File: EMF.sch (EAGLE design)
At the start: 23 parts, among them X1 22-23-2021

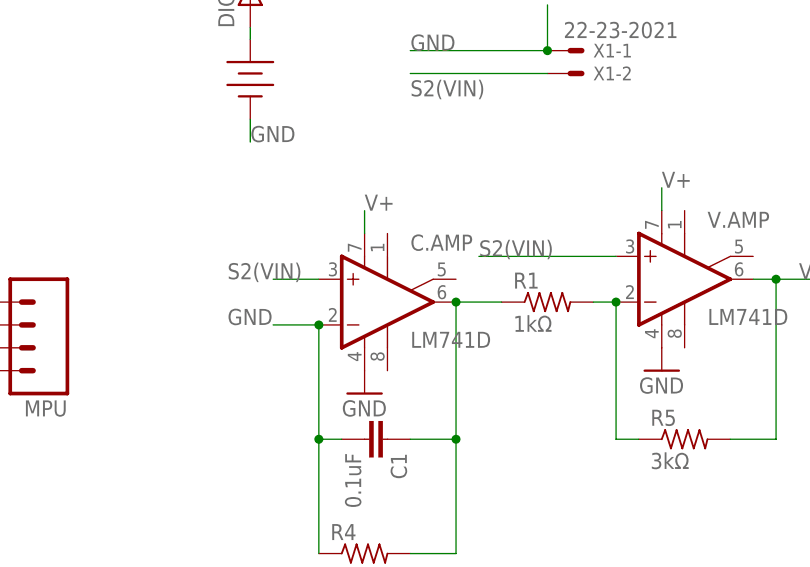
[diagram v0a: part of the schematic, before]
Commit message: fix op-amp connections
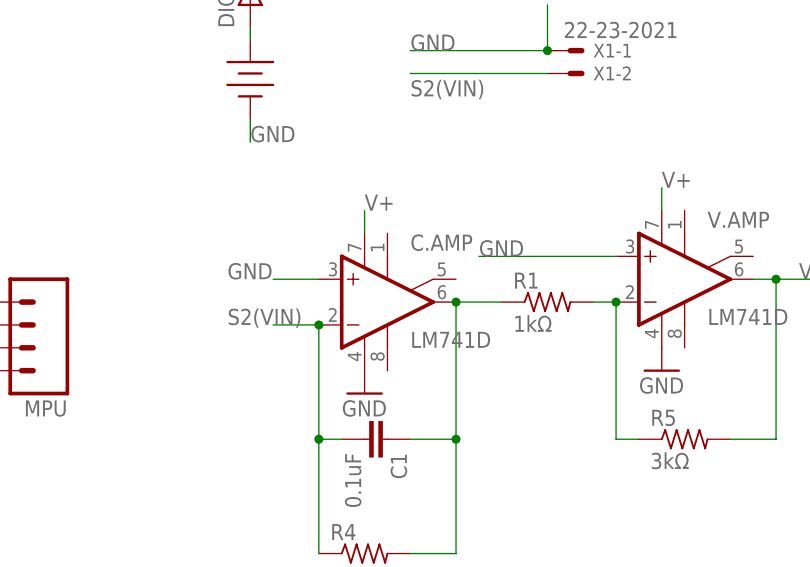
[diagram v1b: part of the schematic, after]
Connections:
- net GND: now also C.AMP.+IN, V.AMP.+IN; no longer C.AMP.-IN, C1.2, R4.1
- net S2(VIN): now also C.AMP.-IN, C1.2, R4.1; no longer C.AMP.+IN, V.AMP.+IN
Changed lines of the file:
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@@
 </segment>
 <segment>
-<pinref part="C.AMP" gate="A" pin="+IN"/>
-<wire x1="30.48" y1="55.88" x2="25.4" y2="55.88" width="0.1524" layer="91"/>
-<label x="20.32" y="55.88" size="1.778" layer="95"/>
-</segment>
-<segment>
-<pinref part="V.AMP" gate="A" pin="+IN"/>
-<wire x1="63.5" y1="58.42" x2="48.26" y2="58.42" width="0.1524" layer="91"/>
-<label x="48.26" y="58.42" size="1.778" layer="95"/>
+<pinref part="C.AMP" gate="A" pin="-IN"/>
+<wire x1="30.48" y1="50.8" x2="25.4" y2="50.8" width="0.1524" layer="91"/>
+<label x="20.32" y="50.8" size="1.778" layer="95"/>
+<wire x1="30.48" y1="50.8" x2="30.48" y2="38.1" width="0.1524" layer="91"/>
+<junction x="30.48" y="50.8"/>
+<pinref part="C1" gate="G$1" pin="2"/>
+<wire x1="30.48" y1="38.1" x2="33.02" y2="38.1" width="0.1524" layer="91"/>
+<pinref part="R4" gate="G$1" pin="1"/>
+<wire x1="30.48" y1="38.1" x2="30.48" y2="25.4" width="0.1524" layer="91"/>
+<junction x="30.48" y="38.1"/>
 </segment>
 </net>
@@
 </segment>
 <segment>
-<pinref part="C.AMP" gate="A" pin="-IN"/>
-<wire x1="30.48" y1="50.8" x2="25.4" y2="50.8" width="0.1524" layer="91"/>
-<label x="20.32" y="50.8" size="1.778" layer="95"/>
-<wire x1="30.48" y1="50.8" x2="30.48" y2="38.1" width="0.1524" layer="91"/>
-<junction x="30.48" y="50.8"/>
-<pinref part="C1" gate="G$1" pin="2"/>
-<wire x1="30.48" y1="38.1" x2="33.02" y2="38.1" width="0.1524" layer="91"/>
-<pinref part="R4" gate="G$1" pin="1"/>
-<wire x1="30.48" y1="38.1" x2="30.48" y2="25.4" width="0.1524" layer="91"/>
-<junction x="30.48" y="38.1"/>
-</segment>
-<segment>
 <pinref part="MPU" gate="G$1" pin="4"/>
 <wire x1="-7.62" y1="45.72" x2="-17.78" y2="45.72" width="0.1524" layer="91"/>
@@
 <label x="104.14" y="-5.08" size="1.778" layer="95"/>
 </segment>
+<segment>
+<pinref part="C.AMP" gate="A" pin="+IN"/>
+<wire x1="30.48" y1="55.88" x2="25.4" y2="55.88" width="0.1524" layer="91"/>
+<label x="20.32" y="55.88" size="1.778" layer="95"/>
+</segment>
+<segment>
+<pinref part="V.AMP" gate="A" pin="+IN"/>
+<wire x1="63.5" y1="58.42" x2="48.26" y2="58.42" width="0.1524" layer="91"/>
+<label x="48.26" y="58.42" size="1.778" layer="95"/>
+</segment>
 </net>

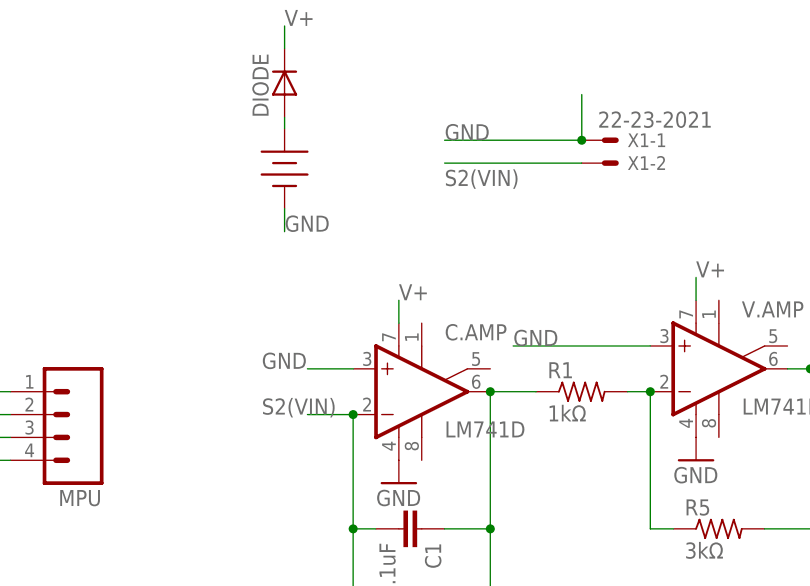
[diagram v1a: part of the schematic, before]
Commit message: fix naming convention
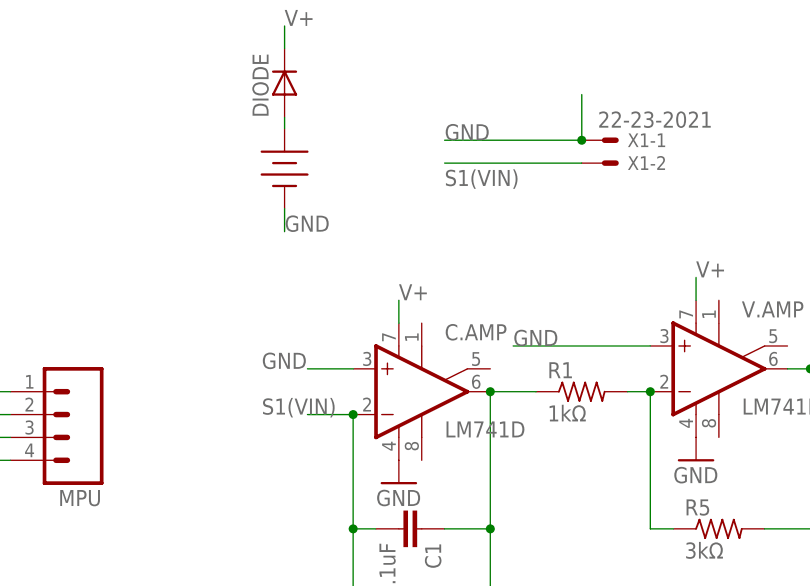
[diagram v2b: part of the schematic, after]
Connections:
- net S2(VIN) renamed S1(VIN)
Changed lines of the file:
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@@
 </busses>
 <nets>
-<net name="S2(VIN)" class="0">
+<net name="S1(VIN)" class="0">
 <segment>
 <pinref part="X1" gate="-2" pin="S"/>
